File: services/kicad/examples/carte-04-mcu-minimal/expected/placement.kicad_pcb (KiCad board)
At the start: 2 copper layers, 38.8 x 30 mm, 15 parts, among them J1 IN_5V, J2 SWD, U1 STM32F103C8T6, U2 AMS1117-3.3

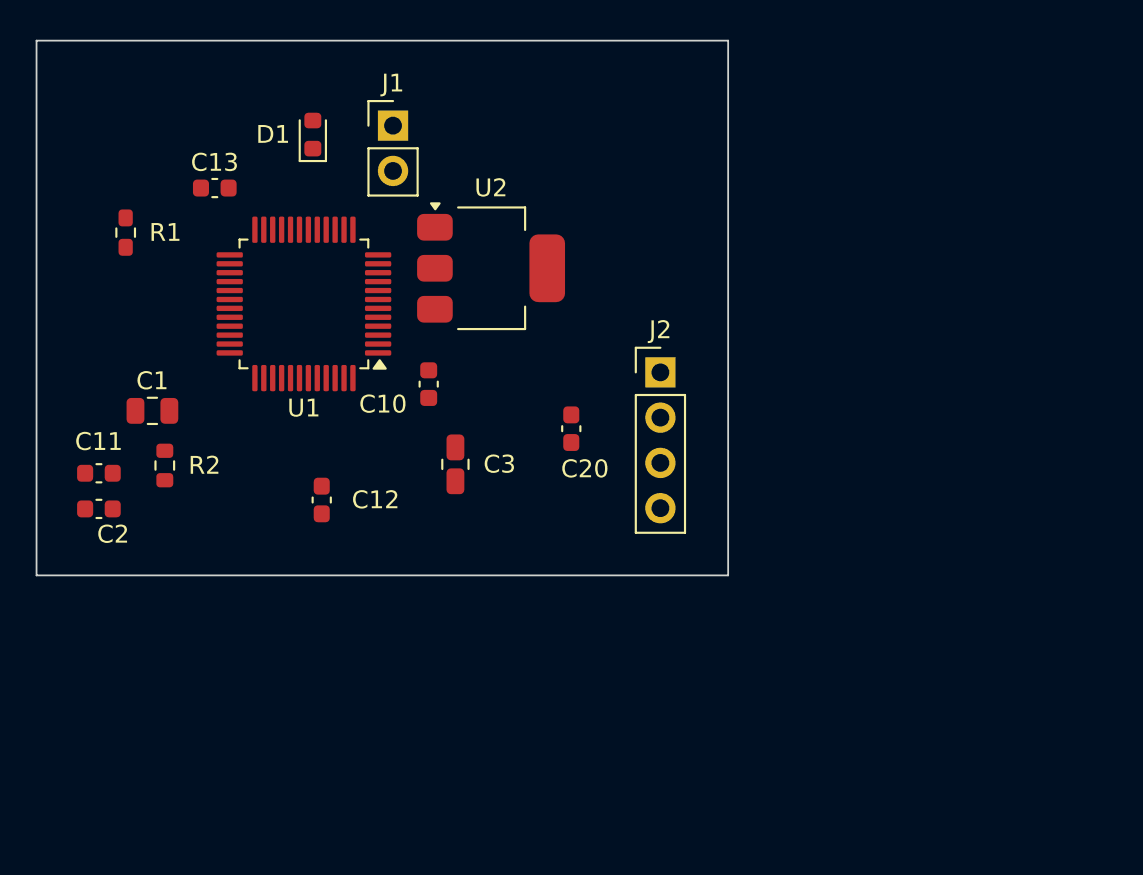
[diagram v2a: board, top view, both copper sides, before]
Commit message: feat(placement): les peripheriques se REPARTISSENT, ils ne s empilent plus
Question de l utilisateur devant le rendu : « c est quoi ce type de placement ? ».
Les composants s entassaient d un seul cote du boitier, etiquettes de
serigraphie l une sur l autre, trois quarts de la couronne vides.

TROIS CAUSES, toutes dans `_poser_les_peripheriques`, toutes la meme faute —
un angle unique pour tout un groupe :

  - les DIRECTS qui visent la meme broche (tous les decouplages d un rail,
    toutes les resistances d un meme signal) recevaient le MEME `angle_vers`
    et le meme rayon de depart ;
  - les SUIVEURS d un meme parent recevaient tous atan2(parent - centre) ;
  - les ISOLES partaient tous de l angle 0.0, c est-a-dire du meme point.

`le_long_du_rayon` ne s ecartait qu une fois la place prise : d ou la file.

REMEDE : `_ecart_en_eventail`. Le PREMIER de chaque groupe garde EXACTEMENT la
direction calculee — c est la topologie, on ne la perd pas pour faire joli — et
les suivants s ecartent symetriquement de 3 x `_PAS_ANGLE_DEG`.
Rien de deja pose ne bouge : seul l ANGLE DE DEPART de la recherche change, et
`le_long_du_rayon` reste seul juge de ce qui est libre.

BANC DES DIX CARTES, contour resserre ET peripheriques repartis :

    carte             demandee    livree         err  manq
    carte-01           25 x 20    20,1 x 13,6     0    0
    carte-02           55 x 40    34,9 x 25,2     0    0
    carte-03           50 x 35    27,6 x 19,9     0    0
    carte-04           60 x 45    36,6 x 29,8     0    0
    carte-05           70 x 50    40,0 x 32,6     0    0
    carte-06           80 x 60    46,5 x 36,4     0    0
    carte-07          110 x 80    47,7 x 38,8     0    0
    carte-08          125 x 95    57,4 x 44,1     0    0
    carte-09          130 x 100   57,8 x 45,2     0    0
    carte-10          140 x 105   59,0 x 45,8     0    0

Dix sur dix, 100 % route. carte-07 gagne 5,5 mm de largeur sur le passage
precedent, carte-06 deux, carte-10 deux. Sur ca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
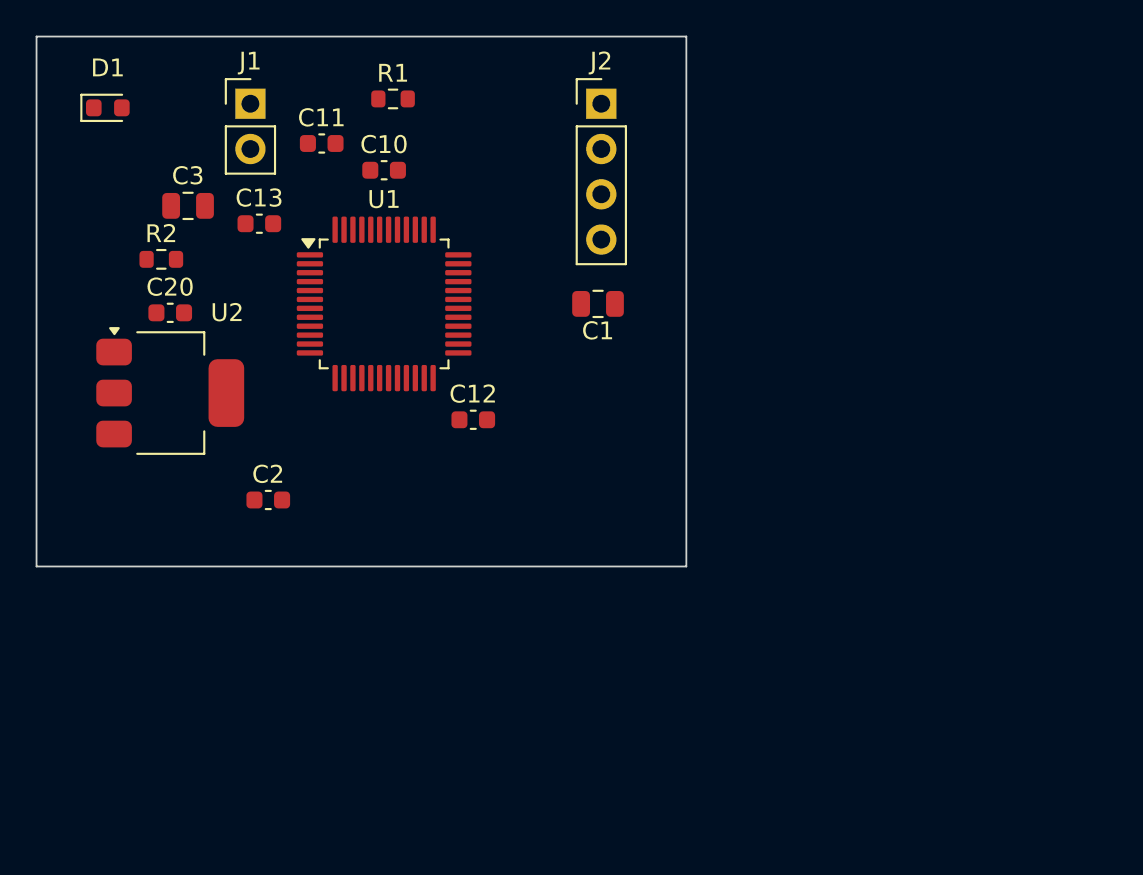
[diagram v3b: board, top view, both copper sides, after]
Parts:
- moved C1 25.7 mm to (150.0, 97.5)
- moved C20 23.4 mm to (126.0, 98.0), turned to 0 degrees
- moved C11 22.3 mm to (134.5, 88.5), turned to 0 degrees
- moved C3 20.9 mm to (127.0, 92.0), turned to 0 degrees
- moved U2 19.3 mm to (126.0, 102.5)
- moved R1 16.8 mm to (138.5, 86.0), turned to 0 degrees
- moved J2 15.4 mm to (150.2, 86.3)
- moved C10 12.3 mm to (138.0, 90.0), turned to 0 degrees
- moved D1 11.6 mm to (122.5, 86.5), turned to 0 degrees
- moved R2 11.6 mm to (125.5, 95.0), turned to 0 degrees
- moved C12 9.62 mm to (143.0, 104.0), turned to 0 degrees
- moved C2 9.51 mm to (131.5, 108.5), turned to 0 degrees
- moved J1 8.09 mm to (130.5, 86.3)
- moved U1 4.50 mm to (138.0, 97.5), turned to 0 degrees
- moved C13 3.20 mm to (131.0, 93.0)
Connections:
- U1 pad 36: Net-(U1-36) -> PWR_FLAG
- U1 pad 48: Net-(U1-48) -> PWR_FLAG
- U1 pad 9: Net-(U1-9) -> PWR_FLAG
- U2 pad 3: VIN -> PWR_FLAG
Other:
- board size 38.8 x 30 mm -> 36.5 x 29.7 mm

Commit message: docs(banc): les dix boards du banc du 2026-09-23, service corrige
Artefacts du banc dont le tableau est deja commite : les dix cartes a
100 % route, 0 erreur, 0 connexion manquante, chacune a la taille de son
circuit.

Co-Authored-By: Claude Opus 5 <noreply@anthropic.com>
Claude-Session: https://claude.ai/code/session_01TnMqm4La2CxQHHB5K8aSSV
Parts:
- moved C10 11.3 mm to (127.0, 92.5)
- moved C3 8.73 mm to (135.0, 88.5)
- moved C11 5.15 mm to (139.0, 91.0)
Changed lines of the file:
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@@
 		(tags "LQFP QFP CASE-932AA CASE-932-03 C48-1 C48-2 C48-3 C48-5 C48-6 C48-6C PT0048A")
 		(property "Reference" "U1"
-			(at 0 -5.85 0)
+			(at -1.6 -5.85 0)
 			(layer "F.SilkS")
 			(effects
@@
 		(generator "kicad-footprint-generator")
 		(layer "F.Cu")
-		(at 127 92)
+		(at 135 88.5)
 		(descr "Capacitor SMD 0805 (2012 Metric), square (rectangular) end terminal, IPC-7351 nominal, (Body size source: IPC-SM-782 page 76, https://www.pcb-3d.com/wordpress/wp-content/uploads/ipc-sm-782a_amendment_1_and_2.pdf, https://docs.google.com/spreadsheets/d/1BsfQQcO9C6DZCsRaXUlFlo91Tg2WpOkGARC1WS5S8t0/edit?usp=sharing)")
 		(tags "capacitor")
@@
 		(generator "kicad-footprint-generator")
 		(layer "F.Cu")
-		(at 138 90)
+		(at 127 92.5)
 		(descr "Capacitor SMD 0603 (1608 Metric), square (rectangular) end terminal, IPC-7351 nominal, (Body size source: IPC-SM-782 page 76, https://www.pcb-3d.com/wordpress/wp-content/uploads/ipc-sm-782a_amendment_1_and_2.pdf)")
 		(tags "capacitor")
@@
 		(generator "kicad-footprint-generator")
 		(layer "F.Cu")
-		(at 134.5 88.5)
+		(at 139 91)
 		(descr "Capacitor SMD 0603 (1608 Metric), square (rectangular) end terminal, IPC-7351 nominal, (Body size source: IPC-SM-782 page 76, https://www.pcb-3d.com/wordpress/wp-content/uploads/ipc-sm-782a_amendment_1_and_2.pdf)")
 		(tags "capacitor")
@@
 		(tags "resistor")
 		(property "Reference" "R2"
-			(at 0 -1.43 0)
-			(layer "F.SilkS")
-			(effects
+			(at -1.6 -1.43 0)
+			(layer "F.SilkS")
+			(effects

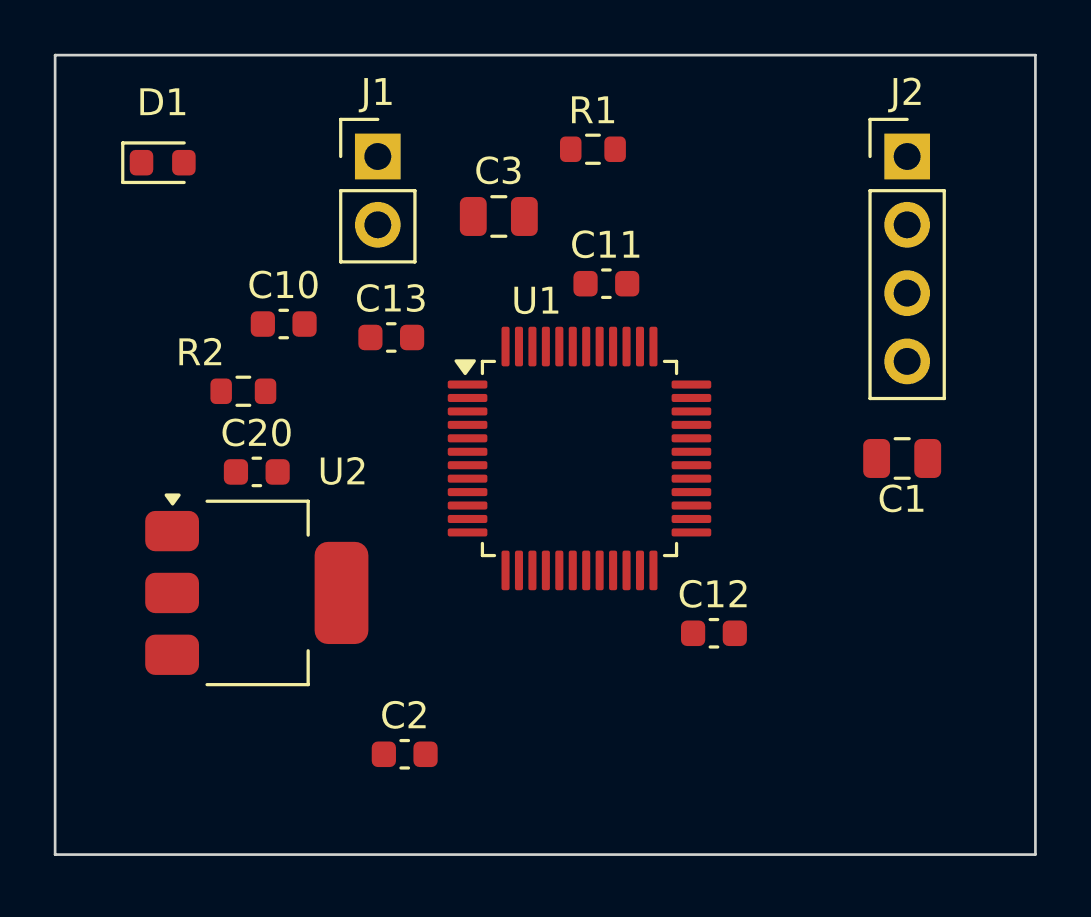
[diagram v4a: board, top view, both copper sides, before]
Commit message: fix(banc): le banc route comme la production — plafond 8, budget du client
D-2026-09-24-f. run_pipeline.py prenait 2 couches et 1800 s par défaut, et
carte-07 écrivait 2 en dur : dix cartes sur quinze ne pouvaient jamais
escalader, et la règle « toute connexion manquante fait monter » était
inerte dans le banc. Mesuré sur carte-07 : 97 %, seule la masse manquante,
« le palier suivant sera tenté »… puis retour à 2 couches.

Plafond par défaut 8 (client Pro Max), budget min(600 + 300 x plafond, 3600)
comme routingSearchBudgetS côté client. En production, rien ne change : le
plafond reste celui du plan.

Livraisons du jour, toutes vérifiées par kicad-cli et contre le schéma
(0 erreur bloquante, 0 connexion manquante, 0 court-circuit) :
carte-04, 05, 06, 08 (campagne de l'après-midi) et carte-09, 10 (4 couches).
Les boards versionnés de ces cartes court-circuitaient des nets du schéma.

Correction de ma propre erreur dans la doc : carte-07 n'avait jamais
escaladé ; les lignes « palier 4 et 6 » du journal étaient celles de
carte-08, démarrée la même minute.

Co-Authored-By: Claude Opus 5.5 <noreply@anthropic.com>
Claude-Session: https://claude.ai/code/session_01TnMqm4La2CxQHHB5K8aSSV
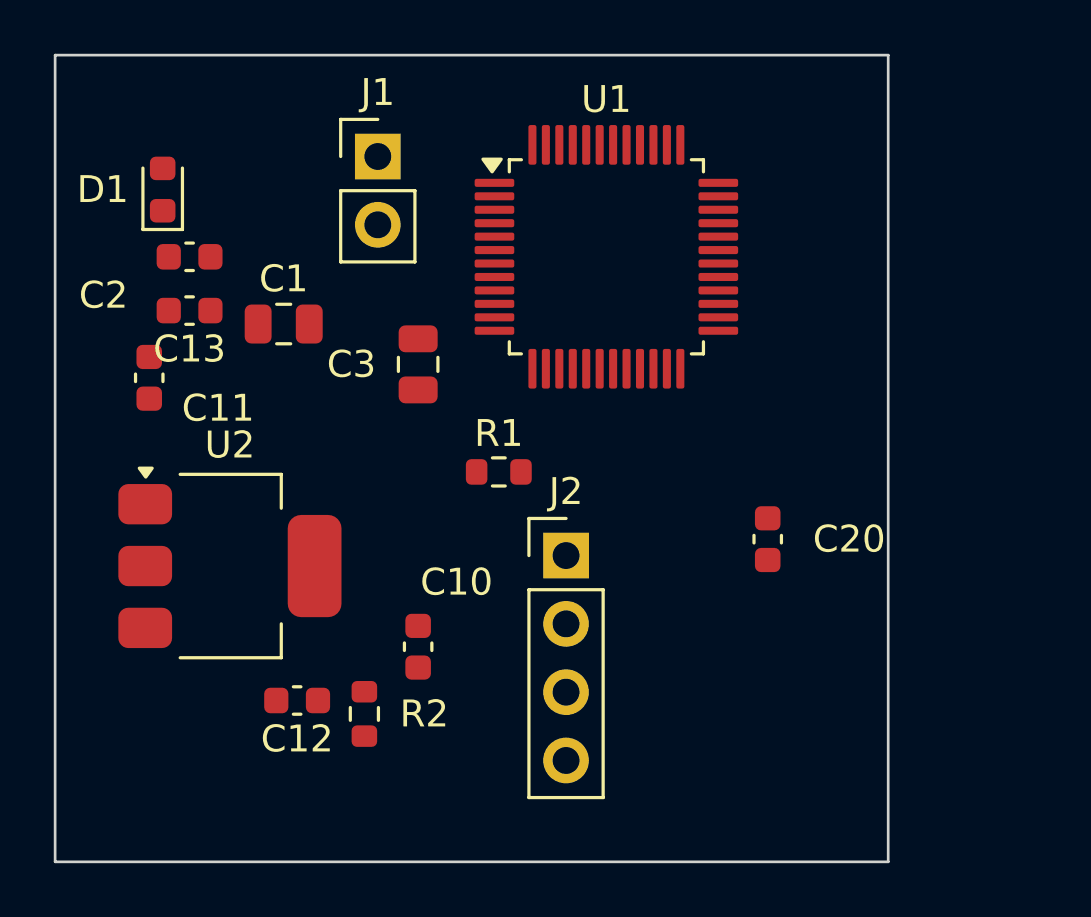
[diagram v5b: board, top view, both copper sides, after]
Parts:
- moved C1 23.5 mm to (127.0, 92.5)
- moved C2 20.2 mm to (123.5, 90.0), turned to 180 degrees
- moved J2 19.5 mm to (137.5, 101.1)
- moved C20 19.2 mm to (145.0, 100.5), turned to 270 degrees
- moved C11 17.4 mm to (122.0, 94.5), turned to 270 degrees
- moved C12 15.7 mm to (127.5, 106.5), turned to 180 degrees
- moved C10 13.0 mm to (132.0, 104.5), turned to 270 degrees
- moved R2 12.8 mm to (130.0, 107.0), turned to 270 degrees
- moved R1 12.5 mm to (135.0, 98.0)
- moved C13 7.57 mm to (123.5, 92.0), turned to 180 degrees
- moved U1 7.57 mm to (139.0, 90.0)
- moved C3 6.26 mm to (132.0, 94.0), turned to 90 degrees
- moved U2 1.41 mm to (125.0, 101.5)
- moved D1 1.00 mm to (122.5, 87.5), turned to 90 degrees
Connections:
- U1 pad 36: PWR_FLAG -> +3V3
- U1 pad 48: PWR_FLAG -> +3V3
- U1 pad 9: PWR_FLAG -> Net-(U1-9)
- U2 pad 3: PWR_FLAG -> VIN
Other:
- board size 36.5 x 29.7 mm -> 31 x 30 mm
